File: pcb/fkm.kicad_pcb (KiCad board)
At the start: 2 copper layers, 50 x 33 mm, 15 parts, among them U1 ESP32-WROOM-32, U2 18650, U3 AMS1117-3.3

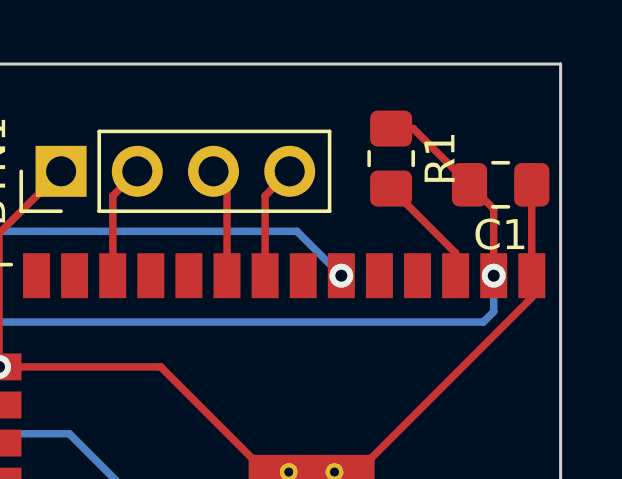
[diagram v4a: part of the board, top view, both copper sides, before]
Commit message: chore(pcb): better capacitor text placement
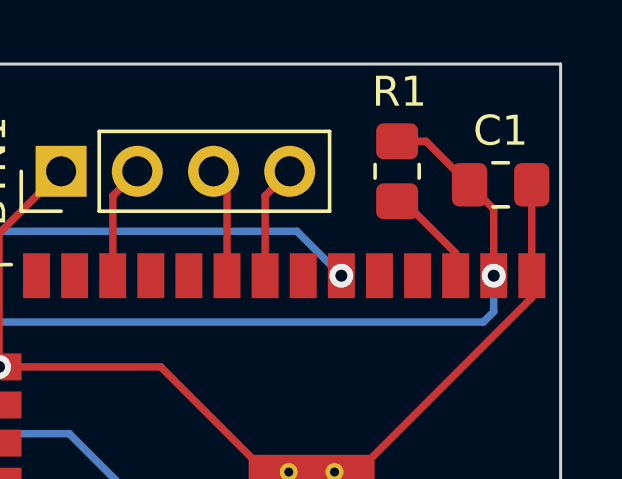
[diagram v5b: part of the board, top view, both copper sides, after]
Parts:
- moved R1 0.47 mm to (138.2, 41.2)
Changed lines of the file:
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@@
 	(footprint "Resistor_SMD:R_0805_2012Metric_Pad1.20x1.40mm_HandSolder"
 		(layer "F.Cu")
-		(at 137.975 40.775 -90)
+		(at 138.175 41.2 -90)
 		(descr "Resistor SMD 0805 (2012 Metric), square (rectangular) end terminal, IPC_7351 nominal with elongated pad for handsoldering. (Body size source: IPC-SM-782 page 72, https://www.pcb-3d.com/wordpress/wp-content/uploads/ipc-sm-782a_amendment_1_and_2.pdf), generated with kicad-footprint-generator")
 		(tags "resistor handsolder")
 		(property "Reference" "R1"
-			(at 0 -1.65 90)
+			(at -2.65 -0.075 180)
 			(layer "F.SilkS")
 			(effects
@@
 			(at 0 1.65 90)
 			(layer "F.Fab")
+			(hide yes)
 			(effects
 				(font
@@
 		(tags "capacitor handsolder")
 		(property "Reference" "C1"
-			(at 0 -1.68 180)
+			(at 0 1.8 180)
 			(layer "F.SilkS")
 			(effects
@@
 			(at 0 1.68 180)
 			(layer "F.Fab")
+			(hide yes)
 			(effects
 				(font
@@
 	)
 	(segment
+		(start 138.175 42.2)
+		(end 138.4 42.2)
+		(width 0.25)
+		(layer "F.Cu")
+		(net 3)
+	)
+	(segment
 		(start 140.125 43.925)
 		(end 140.125 44.68)
@@
 	)
 	(segment
-		(start 137.975 41.775)
+		(start 138.4 42.2)
 		(end 140.125 43.925)
 		(width 0.25)
@@
 	)
 	(segment
-		(start 136.675 69.7)
-		(end 126.8 69.7)
+		(start 139.1375 40.2)
+		(end 140.5875 41.65)
 		(width 0.25)
 		(layer "F.Cu")
@@
 	)
 	(segment
-		(start 140.5875 41.65)
-		(end 141.395 42.4575)
+		(start 136.675 69.7)
+		(end 126.8 69.7)
 		(width 0.25)
 		(layer "F.Cu")
@@
 	)
 	(segment
-		(start 138.7125 39.775)
-		(end 140.5875 41.65)
+		(start 140.5875 41.65)
+		(end 141.395 42.4575)
 		(width 0.25)
 		(layer "F.Cu")
@@
 	)
 	(segment
+		(start 138.175 40.2)
+		(end 139.1375 40.2)
+		(width 0.25)
+		(layer "F.Cu")
+		(net 5)
+	)
+	(segment
 		(start 119.525 53.85)
 		(end 119.45 53.775)
@@
 		(width 0.25)
 		(layer "F.Cu")
-		(net 5)
-	)
-	(segment
-		(start 137.975 39.775)
-		(end 138.7125 39.775)
-		(width 0.25)
-		(layer "F.Cu")

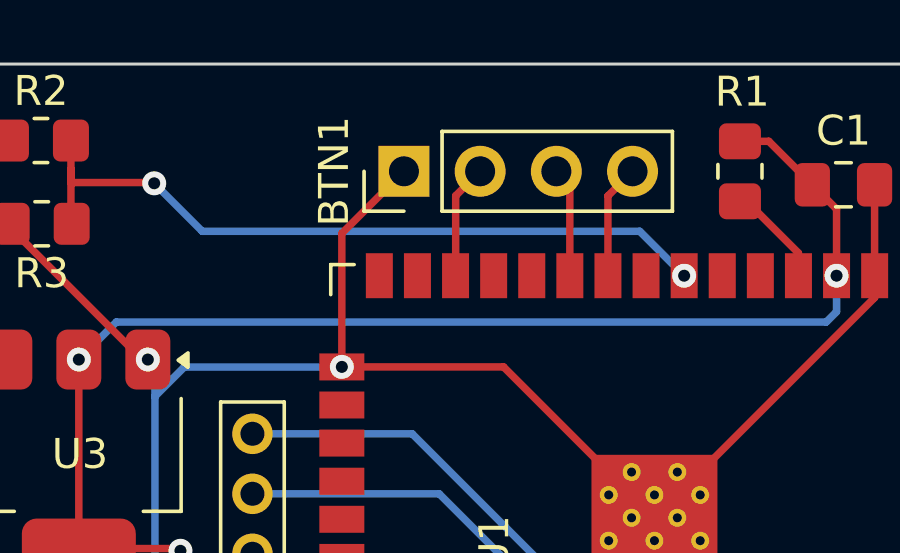
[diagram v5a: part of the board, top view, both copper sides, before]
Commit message: feat(pcb): 4xbuttons output
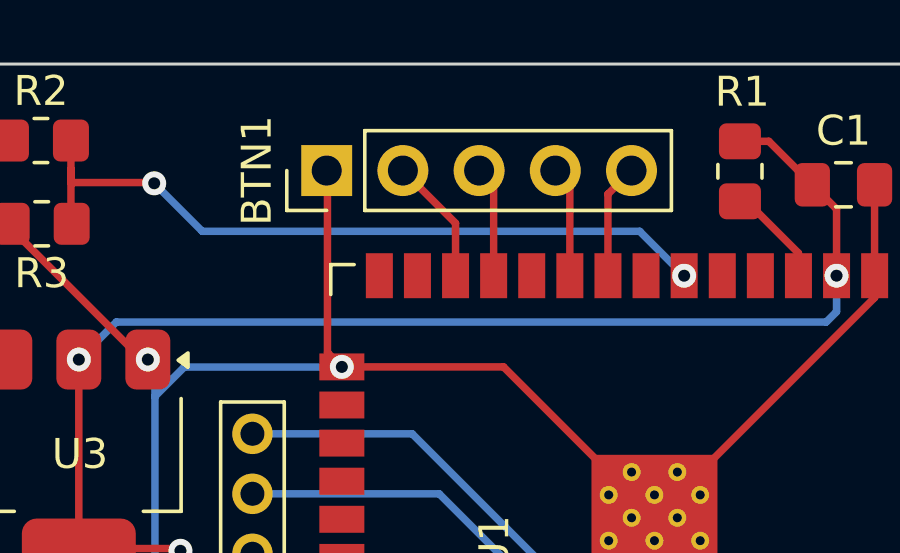
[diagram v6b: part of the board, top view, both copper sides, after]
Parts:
- BTN1: value Conn_01x04 -> Conn_01x05; footprint Connector_PinHeader_2.54mm:PinHeader_1x04_P2.54mm_Vertical -> Connector_PinHeader_2.54mm:PinHeader_1x05_P2.54mm_Vertical
- moved BTN1 2.58 mm to (124.4, 41.2)
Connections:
- BTN1 pad 3: BTN1 -> Net-(BTN1-Pin_3)
- BTN1 pad 4: BTN2 -> BTN1
- U1 pad 11: unconnected-(U1-IO26-Pad11) -> Net-(BTN1-Pin_3)
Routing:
- net Net-(BTN1-Pin_3): track 0.00 -> 3.71 mm
- net GND: track 116.0 -> 115.3 mm
